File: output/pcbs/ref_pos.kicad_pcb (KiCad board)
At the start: 2 copper layers, 125.8 x 86.6 mm, 0 parts

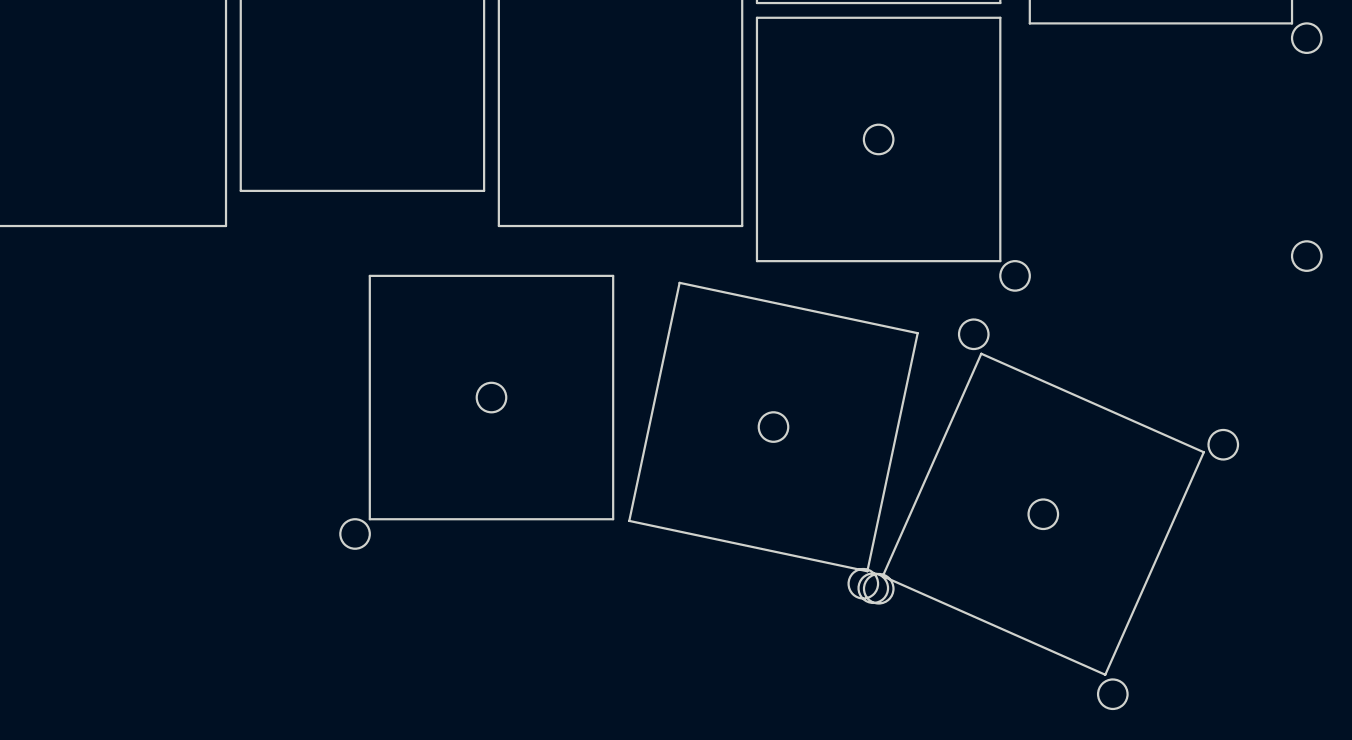
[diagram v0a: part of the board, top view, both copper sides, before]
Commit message: feat: add ring bottom ref
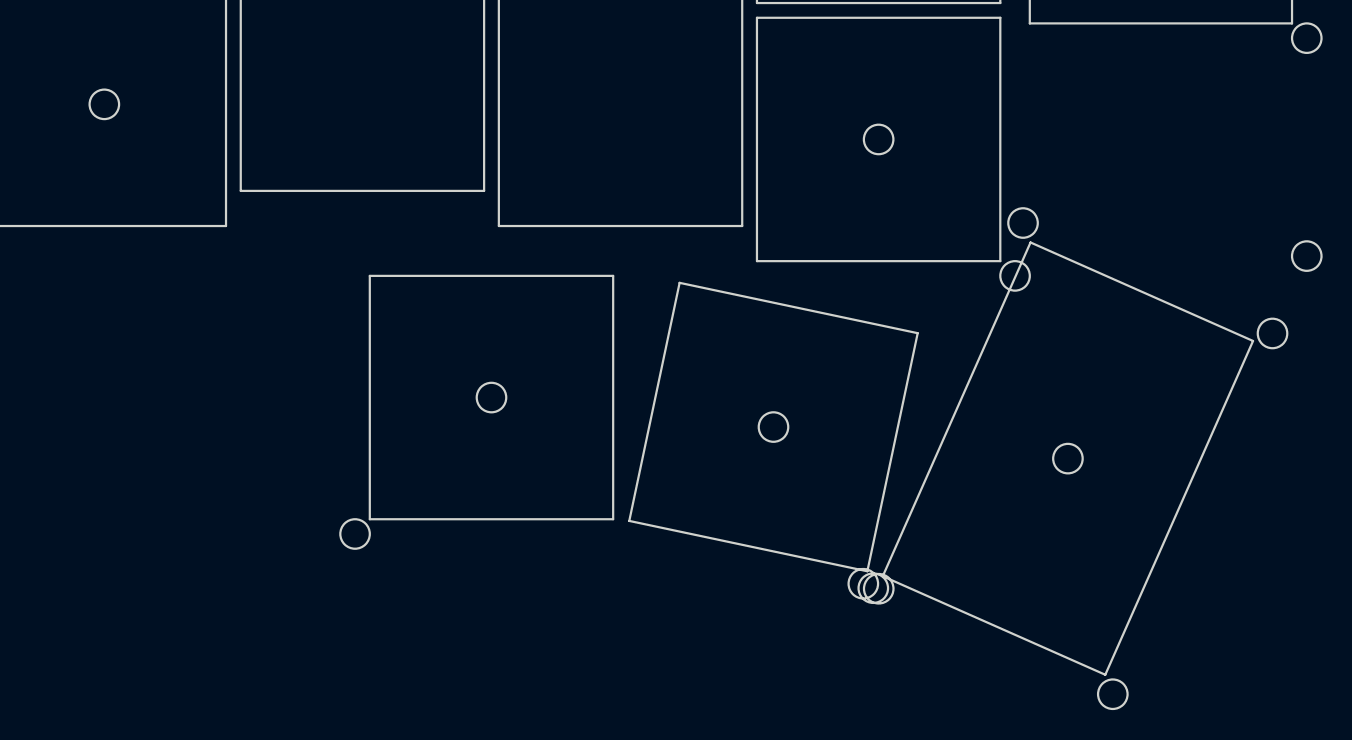
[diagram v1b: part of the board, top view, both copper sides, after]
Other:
- outline, holes or cut-outs redrawn
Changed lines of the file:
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@@
 (gr_line (start 90.14928490000001 10.753881999999999) (end 74.0062659 7.340242199999999) (layer Edge.Cuts) (stroke (width 0.15) (type default)))
 (gr_line (start 74.0062659 7.340242199999999) (end 70.5926261 23.4832612) (layer Edge.Cuts) (stroke (width 0.15) (type default)))
-(gr_line (start 87.7809927 27.234740700000003) (end 102.8685155 33.9143107) (layer Edge.Cuts) (stroke (width 0.15) (type default)))
-(gr_line (start 102.8685155 33.9143107) (end 109.5480855 18.8267879) (layer Edge.Cuts) (stroke (width 0.15) (type default)))
-(gr_line (start 109.5480855 18.8267879) (end 94.4605627 12.147217900000001) (layer Edge.Cuts) (stroke (width 0.15) (type default)))
-(gr_line (start 94.4605627 12.147217900000001) (end 87.7809927 27.234740700000003) (layer Edge.Cuts) (stroke (width 0.15) (type default)))
+(gr_line (start 102.8685155 33.9143107) (end 112.8878705 11.283026500000002) (layer Edge.Cuts) (stroke (width 0.15) (type default)))
+(gr_line (start 87.7809927 27.2347407) (end 97.8003477 4.6034565) (layer Edge.Cuts) (stroke (width 0.15) (type default)))
+(gr_line (start 112.8878705 11.283026500000002) (end 97.8003477 4.6034565) (layer Edge.Cuts) (stroke (width 0.15) (type default)))
+(gr_line (start 87.7809927 27.2347407) (end 102.8685155 33.9143107) (layer Edge.Cuts) (stroke (width 0.15) (type default)))
 (gr_line (start 97.75 -10.25) (end 115.53 -10.25) (layer Edge.Cuts) (stroke (width 0.15) (type default)))
 (gr_line (start 115.53 -10.25) (end 115.53 -43.25) (layer Edge.Cuts) (stroke (width 0.15) (type default)))
@@
 (gr_circle (center 61.25 15.119) (end 62.25 15.119) (layer Edge.Cuts) (stroke (width 0.15) (type default)) (fill none))
 (gr_circle (center 80.37095550000001 17.1185716) (end 81.37095550000001 17.1185716) (layer Edge.Cuts) (stroke (width 0.15) (type default)) (fill none))
-(gr_circle (center 98.6645391 23.0307643) (end 99.6645391 23.0307643) (layer Edge.Cuts) (stroke (width 0.15) (type default)) (fill none))
+(gr_circle (center 100.3344316 19.2588836) (end 101.3344316 19.2588836) (layer Edge.Cuts) (stroke (width 0.15) (type default)) (fill none))
 (gr_circle (center 87.5 -37.381) (end 88.5 -37.381) (layer Edge.Cuts) (stroke (width 0.15) (type default)) (fill none))
 (gr_circle (center 106.64 -26.75) (end 107.64 -26.75) (layer Edge.Cuts) (stroke (width 0.15) (type default)) (fill none))
+(gr_circle (center 35 -4.762) (end 36 -4.762) (layer Edge.Cuts) (stroke (width 0.15) (type default)) (fill none))
 (gr_circle (center 96.75 6.869) (end 97.75 6.869) (layer Edge.Cuts) (stroke (width 0.15) (type default)) (fill none))
 (gr_circle (center 52 24.369) (end 53 24.369) (layer Edge.Cuts) (stroke (width 0.15) (type default)) (fill none))
@@
 (gr_circle (center 103.3780884 35.2335285) (end 104.3780884 35.2335285) (layer Edge.Cuts) (stroke (width 0.15) (type default)) (fill none))
 (gr_circle (center 86.4617749 27.7443136) (end 87.4617749 27.7443136) (layer Edge.Cuts) (stroke (width 0.15) (type default)) (fill none))
-(gr_circle (center 110.8673033 18.317215) (end 111.8673033 18.317215) (layer Edge.Cuts) (stroke (width 0.15) (type default)) (fill none))
-(gr_circle (center 93.9509898 10.8280001) (end 94.9509898 10.8280001) (layer Edge.Cuts) (stroke (width 0.15) (type default)) (fill none))
+(gr_circle (center 114.2070883 10.7734536) (end 115.2070883 10.7734536) (layer Edge.Cuts) (stroke (width 0.15) (type default)) (fill none))
+(gr_circle (center 97.2907749 3.2842387) (end 98.2907749 3.2842387) (layer Edge.Cuts) (stroke (width 0.15) (type default)) (fill none))
 (gr_circle (center 116.53 -9.25) (end 117.53 -9.25) (layer Edge.Cuts) (stroke (width 0.15) (type default)) (fill none))
 (gr_circle (center 116.53 -44.25) (end 117.53 -44.25) (layer Edge.Cuts) (stroke (width 0.15) (type default)) (fill none))

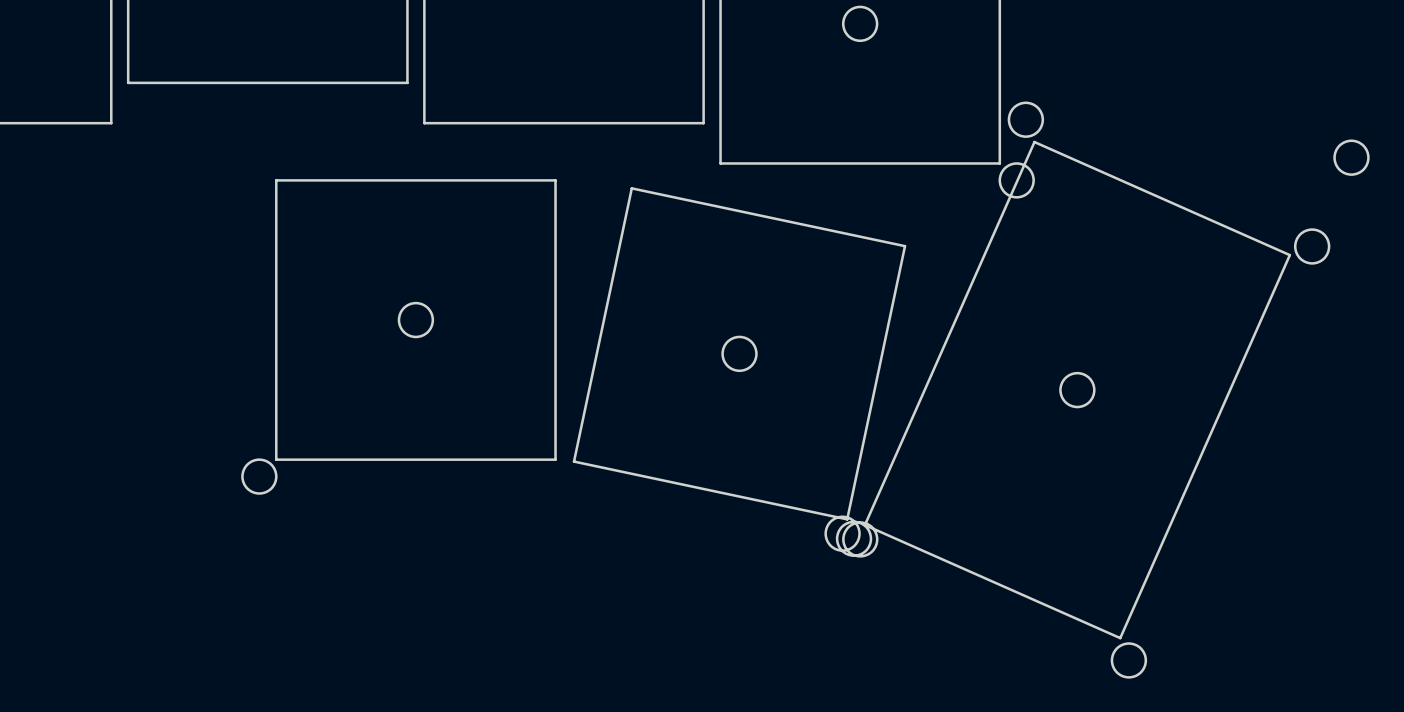
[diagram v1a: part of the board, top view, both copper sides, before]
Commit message: feat: add bottom ring bottom right corner ref
feat: add (bottom inner br, mcu tl) - (inner thumb tr, inner thumb tl)
lines intersection
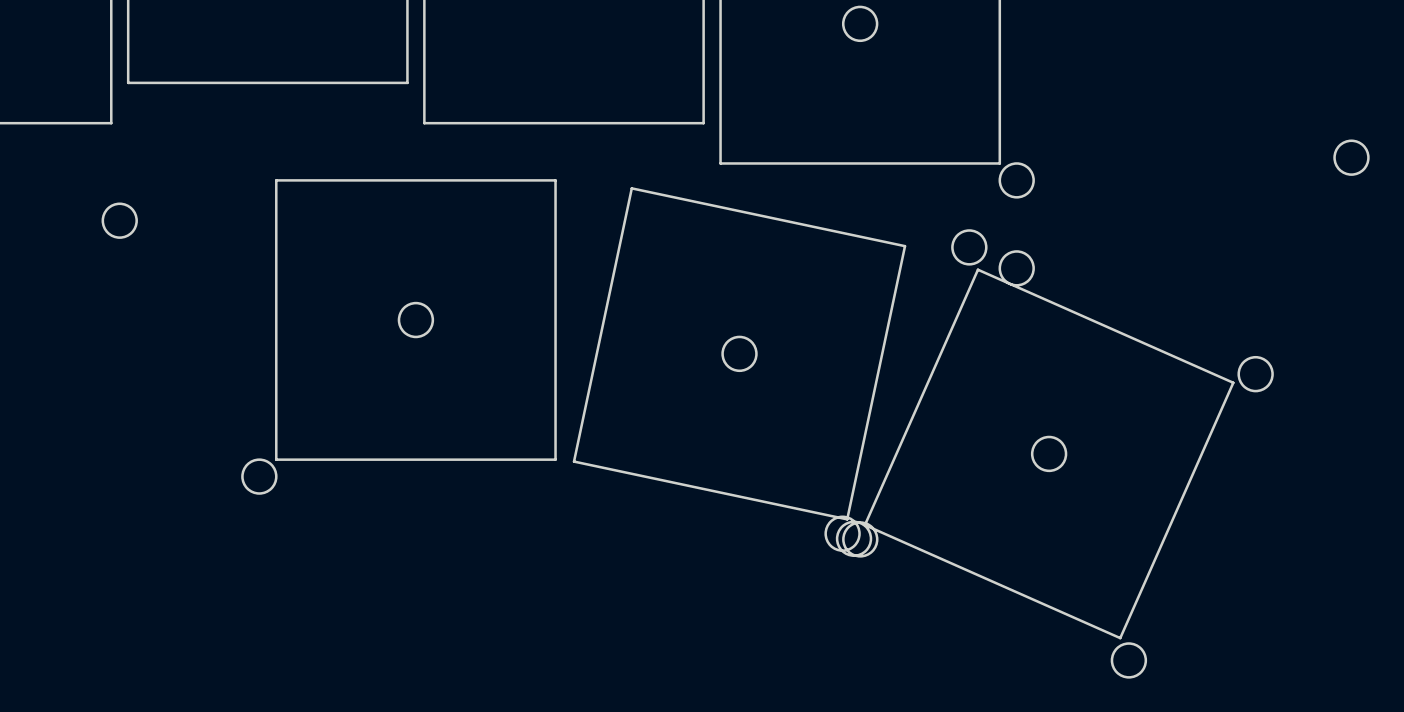
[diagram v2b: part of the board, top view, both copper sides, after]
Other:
- outline, holes or cut-outs redrawn
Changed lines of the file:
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@@
 (gr_line (start 90.14928490000001 10.753881999999999) (end 74.0062659 7.340242199999999) (layer Edge.Cuts) (stroke (width 0.15) (type default)))
 (gr_line (start 74.0062659 7.340242199999999) (end 70.5926261 23.4832612) (layer Edge.Cuts) (stroke (width 0.15) (type default)))
-(gr_line (start 102.8685155 33.9143107) (end 112.8878705 11.283026500000002) (layer Edge.Cuts) (stroke (width 0.15) (type default)))
-(gr_line (start 87.7809927 27.2347407) (end 97.8003477 4.6034565) (layer Edge.Cuts) (stroke (width 0.15) (type default)))
-(gr_line (start 112.8878705 11.283026500000002) (end 97.8003477 4.6034565) (layer Edge.Cuts) (stroke (width 0.15) (type default)))
-(gr_line (start 87.7809927 27.2347407) (end 102.8685155 33.9143107) (layer Edge.Cuts) (stroke (width 0.15) (type default)))
+(gr_line (start 87.7809927 27.234740700000003) (end 102.8685155 33.9143107) (layer Edge.Cuts) (stroke (width 0.15) (type default)))
+(gr_line (start 102.8685155 33.9143107) (end 109.5480855 18.8267879) (layer Edge.Cuts) (stroke (width 0.15) (type default)))
+(gr_line (start 109.5480855 18.8267879) (end 94.4605627 12.147217900000001) (layer Edge.Cuts) (stroke (width 0.15) (type default)))
+(gr_line (start 94.4605627 12.147217900000001) (end 87.7809927 27.234740700000003) (layer Edge.Cuts) (stroke (width 0.15) (type default)))
 (gr_line (start 97.75 -10.25) (end 115.53 -10.25) (layer Edge.Cuts) (stroke (width 0.15) (type default)))
 (gr_line (start 115.53 -10.25) (end 115.53 -43.25) (layer Edge.Cuts) (stroke (width 0.15) (type default)))
@@
 (gr_circle (center 61.25 15.119) (end 62.25 15.119) (layer Edge.Cuts) (stroke (width 0.15) (type default)) (fill none))
 (gr_circle (center 80.37095550000001 17.1185716) (end 81.37095550000001 17.1185716) (layer Edge.Cuts) (stroke (width 0.15) (type default)) (fill none))
-(gr_circle (center 100.3344316 19.2588836) (end 101.3344316 19.2588836) (layer Edge.Cuts) (stroke (width 0.15) (type default)) (fill none))
+(gr_circle (center 98.6645391 23.0307643) (end 99.6645391 23.0307643) (layer Edge.Cuts) (stroke (width 0.15) (type default)) (fill none))
 (gr_circle (center 87.5 -37.381) (end 88.5 -37.381) (layer Edge.Cuts) (stroke (width 0.15) (type default)) (fill none))
 (gr_circle (center 106.64 -26.75) (end 107.64 -26.75) (layer Edge.Cuts) (stroke (width 0.15) (type default)) (fill none))
@@
 (gr_circle (center 103.3780884 35.2335285) (end 104.3780884 35.2335285) (layer Edge.Cuts) (stroke (width 0.15) (type default)) (fill none))
 (gr_circle (center 86.4617749 27.7443136) (end 87.4617749 27.7443136) (layer Edge.Cuts) (stroke (width 0.15) (type default)) (fill none))
-(gr_circle (center 114.2070883 10.7734536) (end 115.2070883 10.7734536) (layer Edge.Cuts) (stroke (width 0.15) (type default)) (fill none))
-(gr_circle (center 97.2907749 3.2842387) (end 98.2907749 3.2842387) (layer Edge.Cuts) (stroke (width 0.15) (type default)) (fill none))
+(gr_circle (center 110.8673033 18.317215) (end 111.8673033 18.317215) (layer Edge.Cuts) (stroke (width 0.15) (type default)) (fill none))
+(gr_circle (center 93.9509898 10.8280001) (end 94.9509898 10.8280001) (layer Edge.Cuts) (stroke (width 0.15) (type default)) (fill none))
 (gr_circle (center 116.53 -9.25) (end 117.53 -9.25) (layer Edge.Cuts) (stroke (width 0.15) (type default)) (fill none))
 (gr_circle (center 116.53 -44.25) (end 117.53 -44.25) (layer Edge.Cuts) (stroke (width 0.15) (type default)) (fill none))
 (gr_circle (center 96.75 -44.25) (end 97.75 -44.25) (layer Edge.Cuts) (stroke (width 0.15) (type default)) (fill none))
+(gr_circle (center 43.75 9.25) (end 44.75 9.25) (layer Edge.Cuts) (stroke (width 0.15) (type default)) (fill none))
+(gr_circle (center 96.75 12.067182) (end 97.75 12.067182) (layer Edge.Cuts) (stroke (width 0.15) (type default)) (fill none))
 (gr_circle (center 87.1375839 28.0435087) (end 88.1375839 28.0435087) (layer Edge.Cuts) (stroke (width 0.15) (type default)) (fill none))
 (gr_circle (center 116.53 5.5265615) (end 117.53 5.5265615) (layer Edge.Cuts) (stroke (width 0.15) (type default)) (fill none))
